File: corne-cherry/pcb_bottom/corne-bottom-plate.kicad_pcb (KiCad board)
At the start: 2 copper layers, 152.8 x 91.4 mm, 5 parts

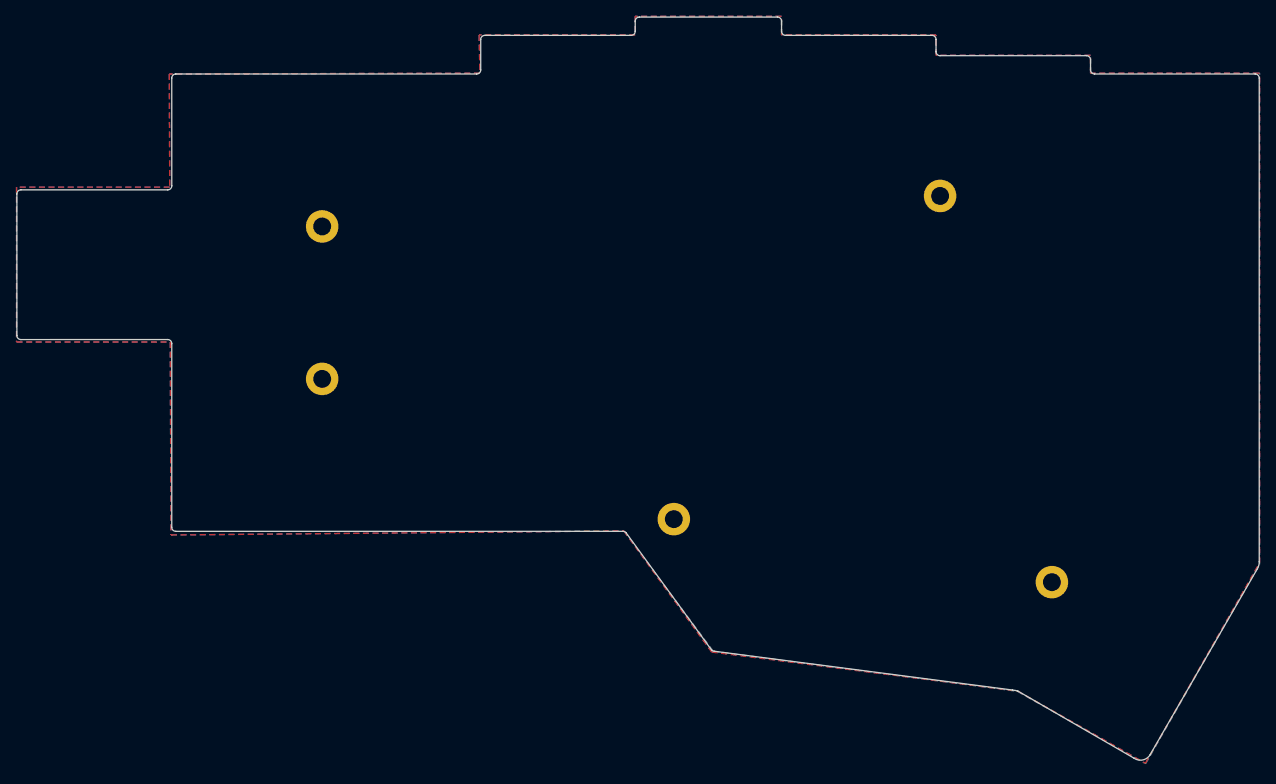
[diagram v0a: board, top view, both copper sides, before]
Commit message: fixed outlines for pcb plates
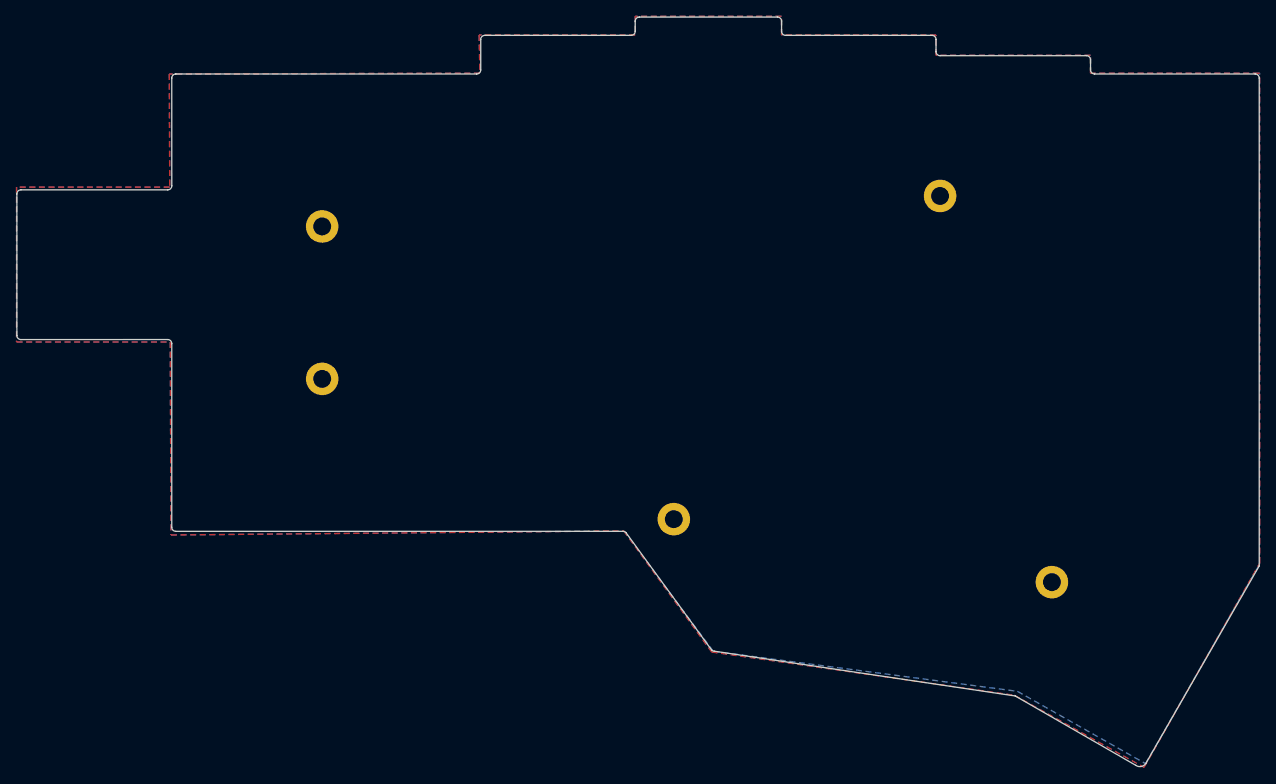
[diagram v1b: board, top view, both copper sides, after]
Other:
- board size 152.8 x 91.4 mm -> 152.8 x 92.2 mm
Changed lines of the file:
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@@
-(kicad_pcb (version 20171130) (host pcbnew "(5.1.0)-1")
+(kicad_pcb (version 20171130) (host pcbnew "(5.1.8)-1")
   (general
     (thickness 1.6)
-    (drawings 59)
+    (drawings 57)
     (tracks 0)
     (zones 0)
@@
       (effects (font (size 1 1) (thickness 0.15)))
     )
-    (fp_text user %R (at 0.3 0) (layer F.Fab)
-      (effects (font (size 1 1) (thickness 0.15)))
-    )
-    (fp_circle (center 0 0) (end 2.2 0) (layer Cmts.User) (width 0.15))
-    (fp_circle (center 0 0) (end 2.45 0) (layer F.CrtYd) (width 0.05))
+    (fp_circle (center 0 0) (end 2.45 0) (layer F.CrtYd) (width 0.05))
+    (fp_circle (center 0 0) (end 2.2 0) (layer Cmts.User) (width 0.15))
+    (fp_text user %R (at 0.3 0) (layer F.Fab)
+      (effects (font (size 1 1) (thickness 0.15)))
+    )
     (pad "" thru_hole circle (at 0 0) (size 4 4) (drill 2.2) (layers *.Cu *.Mask))
   )
@@
       (effects (font (size 1 1) (thickness 0.15)))
     )
-    (fp_text user %R (at 0.3 0) (layer F.Fab)
-      (effects (font (size 1 1) (thickness 0.15)))
-    )
-    (fp_circle (center 0 0) (end 2.2 0) (layer Cmts.User) (width 0.15))
-    (fp_circle (center 0 0) (end 2.45 0) (layer F.CrtYd) (width 0.05))
+    (fp_circle (center 0 0) (end 2.45 0) (layer F.CrtYd) (width 0.05))
+    (fp_circle (center 0 0) (end 2.2 0) (layer Cmts.User) (width 0.15))
+    (fp_text user %R (at 0.3 0) (layer F.Fab)
+      (effects (font (size 1 1) (thickness 0.15)))
+    )
     (pad "" thru_hole circle (at 0 0) (size 4 4) (drill 2.2) (layers *.Cu *.Mask))
   )
@@
       (effects (font (size 1 1) (thickness 0.15)))
     )
-    (fp_text user %R (at 0.3 0) (layer F.Fab)
-      (effects (font (size 1 1) (thickness 0.15)))
-    )
-    (fp_circle (center 0 0) (end 2.2 0) (layer Cmts.User) (width 0.15))
-    (fp_circle (center 0 0) (end 2.45 0) (layer F.CrtYd) (width 0.05))
+    (fp_circle (center 0 0) (end 2.45 0) (layer F.CrtYd) (width 0.05))
+    (fp_circle (center 0 0) (end 2.2 0) (layer Cmts.User) (width 0.15))
+    (fp_text user %R (at 0.3 0) (layer F.Fab)
+      (effects (font (size 1 1) (thickness 0.15)))
+    )
     (pad "" thru_hole circle (at 0 0) (size 4 4) (drill 2.2) (layers *.Cu *.Mask))
   )
@@
       (effects (font (size 1 1) (thickness 0.15)))
     )
-    (fp_text user %R (at 0.3 0) (layer F.Fab)
-      (effects (font (size 1 1) (thickness 0.15)))
-    )
-    (fp_circle (center 0 0) (end 2.2 0) (layer Cmts.User) (width 0.15))
-    (fp_circle (center 0 0) (end 2.45 0) (layer F.CrtYd) (width 0.05))
+    (fp_circle (center 0 0) (end 2.45 0) (layer F.CrtYd) (width 0.05))
+    (fp_circle (center 0 0) (end 2.2 0) (layer Cmts.User) (width 0.15))
+    (fp_text user %R (at 0.3 0) (layer F.Fab)
+      (effects (font (size 1 1) (thickness 0.15)))
+    )
     (pad "" thru_hole circle (at 0 0) (size 4 4) (drill 2.2) (layers *.Cu *.Mask))
   )
@@
       (effects (font (size 1 1) (thickness 0.15)))
     )
-    (fp_text user %R (at 0.3 0) (layer F.Fab)
-      (effects (font (size 1 1) (thickness 0.15)))
-    )
-    (fp_circle (center 0 0) (end 2.2 0) (layer Cmts.User) (width 0.15))
-    (fp_circle (center 0 0) (end 2.45 0) (layer F.CrtYd) (width 0.05))
-    (pad "" thru_hole circle (at 0 0) (size 4 4) (drill 2.2) (layers *.Cu *.Mask))
-  )
+    (fp_circle (center 0 0) (end 2.45 0) (layer F.CrtYd) (width 0.05))
+    (fp_circle (center 0 0) (end 2.2 0) (layer Cmts.User) (width 0.15))
+    (fp_text user %R (at 0.3 0) (layer F.Fab)
+      (effects (font (size 1 1) (thickness 0.15)))
+    )
+    (pad "" thru_hole circle (at 0 0) (size 4 4) (drill 2.2) (layers *.Cu *.Mask))
+  )
+  (gr_line (start 116.853553 124.396447) (end 127.4 138.85) (angle 90) (layer Edge.Cuts) (width 0.15))
+  (gr_arc (start 127.753553 138.496447) (end 127.753553 138.996447) (angle 45) (layer Edge.Cuts) (width 0.15))
   (gr_line (start 169.25 128.05) (end 169.25 132.950063) (layer F.Fab) (width 0.1))
   (gr_line (start 166.8 130.5) (end 171.7 130.5) (layer F.Fab) (width 0.1))
@@
   (gr_line (start 153.05 83) (end 157.95 83) (layer F.Fab) (width 0.1))
   (gr_line (start 155.5 80.55) (end 155.5 85.450063) (layer F.Fab) (width 0.1))
-  (gr_arc (start 193.047765 127.997697) (end 194.522764 128.847696) (angle -30.71750663) (layer Edge.Cuts) (width 0.15))
-  (gr_arc (start 180.14425 151.010957) (end 179.369251 152.160956) (angle -90.22347501) (layer Edge.Cuts) (width 0.15))
-  (gr_arc (start 164.087404 147.16844) (end 165.075 143.9) (angle -11.21335546) (layer Edge.Cuts) (width 0.15))
-  (gr_line (start 181.297263 151.781465) (end 194.522764 128.847696) (layer Edge.Cuts) (width 0.15))
-  (gr_line (start 165.075 143.9) (end 179.369251 152.160956) (layer Edge.Cuts) (width 0.15))
-  (gr_line (start 127.75 139) (end 164.420556 143.770344) (layer Edge.Cuts) (width 0.15))
-  (gr_arc (start 127.75 138.5) (end 127.75 139) (angle 45) (layer Edge.Cuts) (width 0.15))
-  (gr_line (start 116.853553 124.396447) (end 127.396447 138.853553) (angle 90) (layer Edge.Cuts) (width 0.15))
   (gr_line (start 169.26 130.5) (end 169.25 130.5) (angle 90) (layer Eco2.User) (width 2.5))
   (gr_line (start 122.76 122.75) (end 122.75 122.75) (angle 90) (layer Eco2.User) (width 2.5))
@@
   (gr_arc (start 174.5 67.5) (end 174.5 68) (angle 90) (layer Edge.Cuts) (width 0.15))
   (gr_line (start 194.25 68) (end 174.5 68) (angle 90) (layer Edge.Cuts) (width 0.15))
-  (gr_arc (start 116.5 124.75) (end 116.5 124.25) (angle 45) (layer Edge.Cuts) (width 0.15))
   (gr_arc (start 61.5 123.75) (end 61.5 124.25) (angle 90) (layer Edge.Cuts) (width 0.15))
   (gr_arc (start 98.5 67.5) (end 99 67.5) (angle 90) (layer Edge.Cuts) (width 0.15))
@@
   (gr_arc (start 155.5 65.25) (end 155.5 65.75) (angle 90) (layer Edge.Cuts) (width 0.15))
   (gr_arc (start 194.25 68.5) (end 194.25 68) (angle 90) (layer Edge.Cuts) (width 0.15))
-  (gr_line (start 194.75 68.5) (end 194.75 127.975) (angle 90) (layer Edge.Cuts) (width 0.15))
-  (gr_line (start 116.5 124.25) (end 61.5 124.25) (angle 90) (layer Edge.Cuts) (width 0.15))
   (gr_line (start 98.5 68) (end 61.49992 68) (angle 90) (layer Edge.Cuts) (width 0.15))
   (gr_line (start 99 63.75) (end 99 67.5) (angle 90) (layer Edge.Cuts) (width 0.15))
@@
   (gr_line (start 41.94952 100.165) (end 41.94952 82.75) (angle 90) (layer Edge.Cuts) (width 0.15))
   (gr_arc (start 61.49992 68.5) (end 60.99992 68.5) (angle 90) (layer Edge.Cuts) (width 0.15))
+  (gr_arc (start 180.07 152.3) (end 180.8 152.8) (angle 90) (layer Edge.Cuts) (width 0.15))
+  (gr_arc (start 116.5 124.75) (end 116.5 124.25) (angle 45) (layer Edge.Cuts) (width 0.15))
+  (gr_line (start 180.8 152.8) (end 194.75 128.5) (angle 90) (layer Edge.Cuts) (width 0.15))
+  (gr_line (start 164.75 144.5) (end 179.57 153.03) (angle 90) (layer Edge.Cuts) (width 0.15))
+  (gr_line (start 127.753553 138.996447) (end 164.75 144.5) (angle 90) (layer Edge.Cuts) (width 0.15))
+  (gr_line (start 194.75 68.5) (end 194.75 128.5) (angle 90) (layer Edge.Cuts) (width 0.15))
+  (gr_line (start 116.5 124.25) (end 61.5 124.25) (angle 90) (layer Edge.Cuts) (width 0.15))
   (zone (net 0) (net_name "") (layer F.Cu) (hatch edge 0.508)
     (connect_pads (clearance 0.508))
@@
         (xy 136 63.2) (xy 136 60.9) (xy 118 60.9) (xy 118 63.2) (xy 98.8 63.2)
         (xy 98.9 67.9) (xy 60.7 68) (xy 60.749085 81.915743) (xy 41.91 81.915) (xy 41.91 100.965)
-        (xy 60.81628 100.965506) (xy 60.9 124.7) (xy 116.6 124.2) (xy 127.4 139.1) (xy 165.05 143.9)
-        (xy 180.75 152.775) (xy 194.8 128.1) (xy 194.8 67.9)
+        (xy 60.81628 100.965506) (xy 60.9 124.7) (xy 116.6 124.2) (xy 127.4 139.1) (xy 164.616 144.4065)
+        (xy 180.591 153.2815) (xy 194.818 128.143) (xy 194.8 67.9)
       )
     )
